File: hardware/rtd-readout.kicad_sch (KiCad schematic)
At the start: 32 parts, among them J1 Conn_RTD_4W, J4 Conn_T7_Analog, J5 Conn_T7_I2C, J6 Conn_Power, U1 ADS1115IDGS (0x48), U2 ADS1115IDGS (0x49)

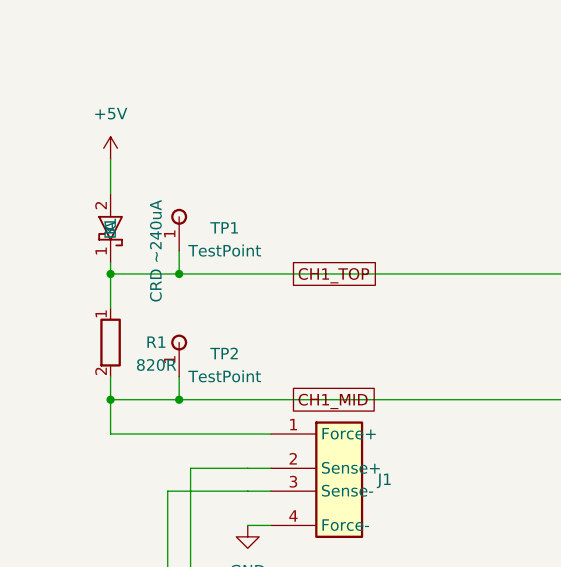
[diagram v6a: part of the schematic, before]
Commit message: rev-F: cryostat/stability respin - 100uA S-101T CRD, C0G sense path, 2ppm R_ref
Sensors are in a vacuum cryostat down to ~100 K; excitation lowered to cut
self-heating ~6x (0.3-1.6 uW nominal), measurement path upgraded to
precision-grade passives. All parts live-verified on Digi-Key with
adversarial fact-checks:
- D1-D4: LIS J500 TO-92 -> SEMITEC S-101T (100uA typ, band 0.05-0.21mA,
  SMD flat 2-lead); custom footprint from SEMITEC's recommended land
  pattern (1.2x1.6mm pads, 3.4mm centers, cathode-band marking).
- R_ref: 820R 10ppm -> 1.00k +/-0.05% +/-2ppm/C (Vishay TNPU12061K00AWEN00);
  V_ref 100mV nom, 210mV = 82% FS at band max. Reference is no longer the
  drift limiter (by design).
- C5-C8: X7R 0805 -> C0G/NP0 0.1uF 50V 1206 (Murata GRM31C5C1H104JA01L);
  moved east of J4 on B.Cu with routed stubs (1206 body cannot straddle
  the pin holes). R7-R14: 1% thick film -> 0.1% 25ppm thin film (Susumu).
- Sims: 100uA/1k/2ppm/VL 2.0/RTD window extended to 100 K (Pt100 29.5R);
  band sweeps 0.5-2.1x; t3 criterion re-gated to 'R_ref not limiting';
  t6 noise assumption made per-read (4-conversion average).

Gates: ERC 0/0, DRC 0 violations / 0 unconnected, SPICE 7/7 PASS.

Co-Authored-By: Claude Fable 5 <noreply@anthropic.com>
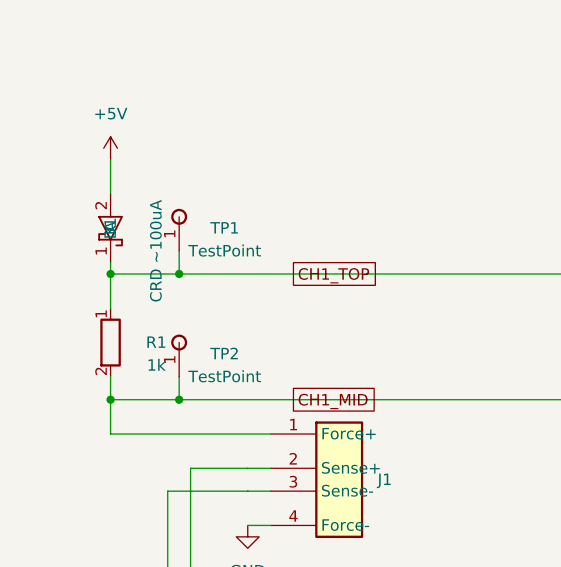
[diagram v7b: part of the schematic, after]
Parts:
- C5, C6, C7, C8: footprint rtd-readout:C_0805_2012Metric -> rtd-readout:C_1206_3216Metric; MPN CL21B104KBCNNNC -> GRM31C5C1H104JA01L; Manufacturer Samsung Electro-Mechanics -> Murata
- D1: value CRD ~240uA -> CRD ~100uA; footprint rtd-readout:TO-92-2_CRD-J500 -> rtd-readout:D_SEMITEC_S-101T; Current_nom ~0.24 mA (J500), +/-20% band (0.192-0.288 mA); stability ov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 -> ~0.10 mA typ (S-101T), band 0.05-0.21 mA (-50%/+110%); stab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; MPN J500 TO-92 2L -> S-101T; Manufacturer Linear Integrated Systems -> SEMITEC; Polarity Pin 1 = K (cathode). Pin 2 = A (anode). J500 TO-92 physical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 -> Pin 1 = K (cathode). Pin 2 = A (anode). S-101T physical: th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
- R1: value 820R -> 1k; MPN RN73H2BTTD8200B10 -> TNPU12061K00AWEN00
- R10, R11, R12, R13, R14, R7, R8, R9: MPN RC0805FR-071KL -> RG2012P-102-B-T5; Manufacturer Yageo -> Susumu
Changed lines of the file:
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@@
 			)
 		)
-		(property "Value" "CRD ~240uA"
+		(property "Value" "CRD ~100uA"
 			(at 43.18 48.26 0)
 			(show_name no)
@@
 			)
 		)
-		(property "Footprint" "rtd-readout:TO-92-2_CRD-J500"
+		(property "Footprint" "rtd-readout:D_SEMITEC_S-101T"
 			(at 38.1 45.72 0)
 			(show_name no)
@@
 			)
 		)
-		(property "Datasheet" "https://www.linearsystems.com/currentregulatingdiodes/j500-series"
+		(property "Datasheet" "https://www.semitec-global.com/uploads/2022/01/P22-23-CRD.pdf"
 			(at 38.1 45.72 0)
 			(show_name no)
@@
 			)
 		)
-		(property "Description" "Current-regulator diode (constant-current diode), ~0.24 mA (LIS J500, 0.192-0.288 mA band), two-terminal, TO-92 2-lead THT. Sets the per-channel excitation current; exact value is measured live and cancels (board_spec.md). Anode -> +V rail, cathode -> R_ref."
+		(property "Description" "Current-regulator diode (constant-current diode), ~0.10 mA (SEMITEC S-101T, 0.05-0.21 mA band), two-terminal, SMD flat 2-lead. rev-F: current lowered ~2.4x to cut RTD self-heating in the vacuum cryostat (sensors to ~100 K). Exact value is measured live and cancels (board_spec.md). Anode -> +V rail, cathode -> R_ref."
 			(at 38.1 45.72 0)
 			(show_name no)
@@
 			)
 		)
-		(property "MPN" "J500 TO-92 2L"
+		(property "MPN" "S-101T"
 			(at 38.1 45.72 0)
 			(show_name no)
@@
 			)
 		)
-		(property "Manufacturer" "Linear Integrated Systems"
+		(property "Manufacturer" "SEMITEC"
 			(at 38.1 45.72 0)
 			(show_name no)
@@
 			)
 		)
-		(property "Polarity" "Pin 1 = K (cathode). Pin 2 = A (anode). J500 TO-92 physical: facing the flat/marked face, left lead = A, right lead = K; the TO-92-2_CRD-J500 footprint silk is mirrored so matching the flat face to the silk outline puts K in pad 1."
+		(property "Polarity" "Pin 1 = K (cathode). Pin 2 = A (anode). S-101T physical: the CATHODE end carries a hatched band on the marked (top) face; place that band toward pad 1 (the silk bar + K marker side)."
 			(at 38.1 45.72 0)
 			(show_name no)
@@
 			)
 		)
-		(property "Current_nom" "~0.24 mA (J500), +/-20% band (0.192-0.288 mA); stability over one scan is what matters, not absolute value."
+		(property "Current_nom" "~0.10 mA typ (S-101T), band 0.05-0.21 mA (-50%/+110%); stability over one scan is what matters, not absolute value (huge spread and up to +2.1%/C Ip tempco are cancelled by the ratiometric readout)."
 			(at 38.1 45.72 0)
 			(show_name no)
@@
 			)
 		)
-		(property "ki_keywords" "CRD current regulator diode constant current J500 RTD excitation TO-92"
+		(property "ki_keywords" "CRD current regulator diode constant current SEMITEC S-101T RTD excitation SMD"
 			(at 38.1 45.72 0)
 			(show_name no)
@@
 			)
 		)
-		(property "ki_fp_filters" "TO?92*"
+		(property "ki_fp_filters" "D_SEMITEC*"
 			(at 38.1 45.72 0)
 			(show_name no)
@@
 			)
 		)
-		(property "Value" "820R"
+		(property "Value" "1k"
 			(at 43.18 60.96 0)
 			(show_name no)
@@
 			)
 		)
-		(property "Datasheet" "https://www.koaspeer.com/pdfs/RN73H.pdf"
+		(property "Datasheet" "https://www.vishay.com/docs/28779/tnpue3.pdf"
 			(at 38.1 58.42 0)
 			(show_name no)
@@
 			)
 		)
-		(property "Description" "Reference resistor for ratiometric current sense. 820 ohm sets V_ref ~197 mV nominal, <=236 mV at the J500 guaranteed-max 0.288 mA, inside the ADS1115 +/-0.256 V range. BINDING SPEC = tempco/stability, NOT absolute value (cross-cal constant C absorbs the value; board_spec.md s.R_ref)."
+		(property "Description" "Reference resistor for ratiometric current sense. 1.00 kohm sets V_ref ~100 mV nominal, <=210 mV at the S-101T band max 0.21 mA, inside the ADS1115 +/-0.256 V range. rev-F part is +/-2 ppm/C so R_ref is no longer the drift limiter. BINDING SPEC = tempco/stability, NOT absolute value (cross-cal absorbs the value; board_spec.md s.R_ref)."
 			(at 38.1 58.42 0)
 			(show_name no)
@@
 			)
 		)
-		(property "MPN" "RN73H2BTTD8200B10"
+		(property "MPN" "TNPU12061K00AWEN00"
 			(at 38.1 58.42 0)
 			(show_name no)
@@
 			)
 		)
-		(property "MPN" "RC0805FR-071KL"
+		(property "MPN" "RG2012P-102-B-T5"
 			(at 111.76 158.75 0)
 			(show_name no)
@@
 			)
 		)
-		(property "Manufacturer" "Yageo"
+		(property "Manufacturer" "Susumu"
 			(at 111.76 158.75 0)
 			(show_name no)
@@
 			)
 		)
-		(property "MPN" "RC0805FR-071KL"
+		(property "MPN" "RG2012P-102-B-T5"
 			(at 140.97 158.75 0)
 			(show_name no)
@@
 			)
 		)
-		(property "Manufacturer" "Yageo"
+		(property "Manufacturer" "Susumu"
 			(at 140.97 158.75 0)
 			(show_name no)
@@
 			)
 		)
-		(property "Footprint" "rtd-readout:C_0805_2012Metric"
+		(property "Footprint" "rtd-readout:C_1206_3216Metric"
 			(at 176.53 160.02 0)
 			(show_name no)
@@
 			)
 		)
-		(property "Description" "Generic non-polarized chip capacitor, 0805. Use for per-ADS1115 VDD decoupling (0.1 uF) and general bypass."
+		(property "Description" "Sense-line differential filter capacitor, 0.1 uF C0G/NP0 (Class 1: no DC-bias/temperature capacitance drift, no piezo, negligible dielectric absorption), 1206, 50 V. rev-F precision upgrade; sits directly in the measurement path with the 1 kohm filter resistors."
 			(at 176.53 160.02 0)
 			(show_name no)
@@
 			)
 		)
-		(property "MPN" "CL21B104KBCNNNC"
+		(property "MPN" "GRM31C5C1H104JA01L"
 			(at 176.53 160.02 0)
 			(show_name no)
@@
 			)
 		)
-		(property "Manufacturer" "Samsung Electro-Mechanics"
+		(property "Manufacturer" "Murata"
 			(at 176.53 160.02 0)
 			(show_name no)
@@
 			)
 		)
-		(property "MPN" "RC0805FR-071KL"
+		(property "MPN" "RG2012P-102-B-T5"
 			(at 111.76 162.56 0)
 			(show_name no)
@@
 			)
 		)
-		(property "Manufacturer" "Yageo"
+		(property "Manufacturer" "Susumu"
 			(at 111.76 162.56 0)
 			(show_name no)
@@
 			)
 		)
-		(property "MPN" "RC0805FR-071KL"
+		(property "MPN" "RG2012P-102-B-T5"
 			(at 140.97 162.56 0)
 			(show_name no)
@@
 			)
 		)
-		(property "Manufacturer" "Yageo"
+		(property "Manufacturer" "Susumu"
 			(at 140.97 162.56 0)
 			(show_name no)
@@
 			)
 		)
-		(property "Footprint" "rtd-readout:C_0805_2012Metric"
+		(property "Footprint" "rtd-readout:C_1206_3216Metric"
 			(at 176.53 163.83 0)
 			(show_name no)
@@
 			)
 		)
-		(property "Description" "Generic non-polarized chip capacitor, 0805. Use for per-ADS1115 VDD decoupling (0.1 uF) and general bypass."
+		(property "Description" "Sense-line differential filter capacitor, 0.1 uF C0G/NP0 (Class 1: no DC-bias/temperature capacitance drift, no piezo, negligible dielectric absorption), 1206, 50 V. rev-F precision upgrade; sits directly in the measurement path with the 1 kohm filter resistors."
 			(at 176.53 163.83 0)
 			(show_name no)
@@
 			)
 		)
-		(property "MPN" "CL21B104KBCNNNC"
+		(property "MPN" "GRM31C5C1H104JA01L"
 			(at 176.53 163.83 0)
 			(show_name no)
@@
 			)
 		)
-		(property "Manufacturer" "Samsung Electro-Mechanics"
+		(property "Manufacturer" "Murata"
 			(at 176.53 163.83 0)
 			(show_name no)
@@
 			)
 		)
-		(property "MPN" "RC0805FR-071KL"
+		(property "MPN" "RG2012P-102-B-T5"
 			(at 111.76 166.37 0)
 			(show_name no)
@@
 			)
 		)
-		(property "Manufacturer" "Yageo"
+		(property "Manufacturer" "Susumu"
 			(at 111.76 166.37 0)
 			(show_name no)
@@
 			)
 		)
-		(property "MPN" "RC0805FR-071KL"
+		(property "MPN" "RG2012P-102-B-T5"
 			(at 140.97 166.37 0)
 			(show_name no)
@@
 			)
 		)
-		(property "Manufacturer" "Yageo"
+		(property "Manufacturer" "Susumu"
 			(at 140.97 166.37 0)
 			(show_name no)
@@
 			)
 		)
-		(property "Footprint" "rtd-readout:C_0805_2012Metric"
+		(property "Footprint" "rtd-readout:C_1206_3216Metric"
 			(at 176.53 167.64 0)
 			(show_name no)
@@
 			)
 		)
-		(property "Description" "Generic non-polarized chip capacitor, 0805. Use for per-ADS1115 VDD decoupling (0.1 uF) and general bypass."
+		(property "Description" "Sense-line differential filter capacitor, 0.1 uF C0G/NP0 (Class 1: no DC-bias/temperature capacitance drift, no piezo, negligible dielectric absorption), 1206, 50 V. rev-F precision upgrade; sits directly in the measurement path with the 1 kohm filter resistors."
 			(at 176.53 167.64 0)
 			(show_name no)
@@
 			)
 		)
-		(property "MPN" "CL21B104KBCNNNC"
+		(property "MPN" "GRM31C5C1H104JA01L"
 			(at 176.53 167.64 0)
 			(show_name no)
@@
 			)
 		)
-		(property "Manufacturer" "Samsung Electro-Mechanics"
+		(property "Manufacturer" "Murata"
 			(at 176.53 167.64 0)
 			(show_name no)
@@
 			)
 		)
-		(property "MPN" "RC0805FR-071KL"
+		(property "MPN" "RG2012P-102-B-T5"
 			(at 111.76 173.99 0)
 			(show_name no)
@@
 			)
 		)
-		(property "Manufacturer" "Yageo"
+		(property "Manufacturer" "Susumu"
 			(at 111.76 173.99 0)
 			(show_name no)
@@
 			)
 		)
-		(property "MPN" "RC0805FR-071KL"
+		(property "MPN" "RG2012P-102-B-T5"
 			(at 140.97 173.99 0)
 			(show_name no)
@@
 			)
 		)
-		(property "Manufacturer" "Yageo"
+		(property "Manufacturer" "Susumu"
 			(at 140.97 173.99 0)
 			(show_name no)
@@
 			)
 		)
-		(property "Footprint" "rtd-readout:C_0805_2012Metric"
+		(property "Footprint" "rtd-readout:C_1206_3216Metric"
 			(at 176.53 175.26 0)
 			(show_name no)
@@
 			)
 		)
-		(property "Description" "Generic non-polarized chip capacitor, 0805. Use for per-ADS1115 VDD decoupling (0.1 uF) and general bypass."
+		(property "Description" "Sense-line differential filter capacitor, 0.1 uF C0G/NP0 (Class 1: no DC-bias/temperature capacitance drift, no piezo, negligible dielectric absorption), 1206, 50 V. rev-F precision upgrade; sits directly in the measurement path with the 1 kohm filter resistors."
 			(at 176.53 175.26 0)
 			(show_name no)
@@
 			)
 		)
-		(property "MPN" "CL21B104KBCNNNC"
+		(property "MPN" "GRM31C5C1H104JA01L"
 			(at 176.53 175.26 0)
 			(show_name no)
@@
 			)
 		)
-		(property "Manufacturer" "Samsung Electro-Mechanics"
+		(property "Manufacturer" "Murata"
 			(at 176.53 175.26 0)
 			(show_name no)

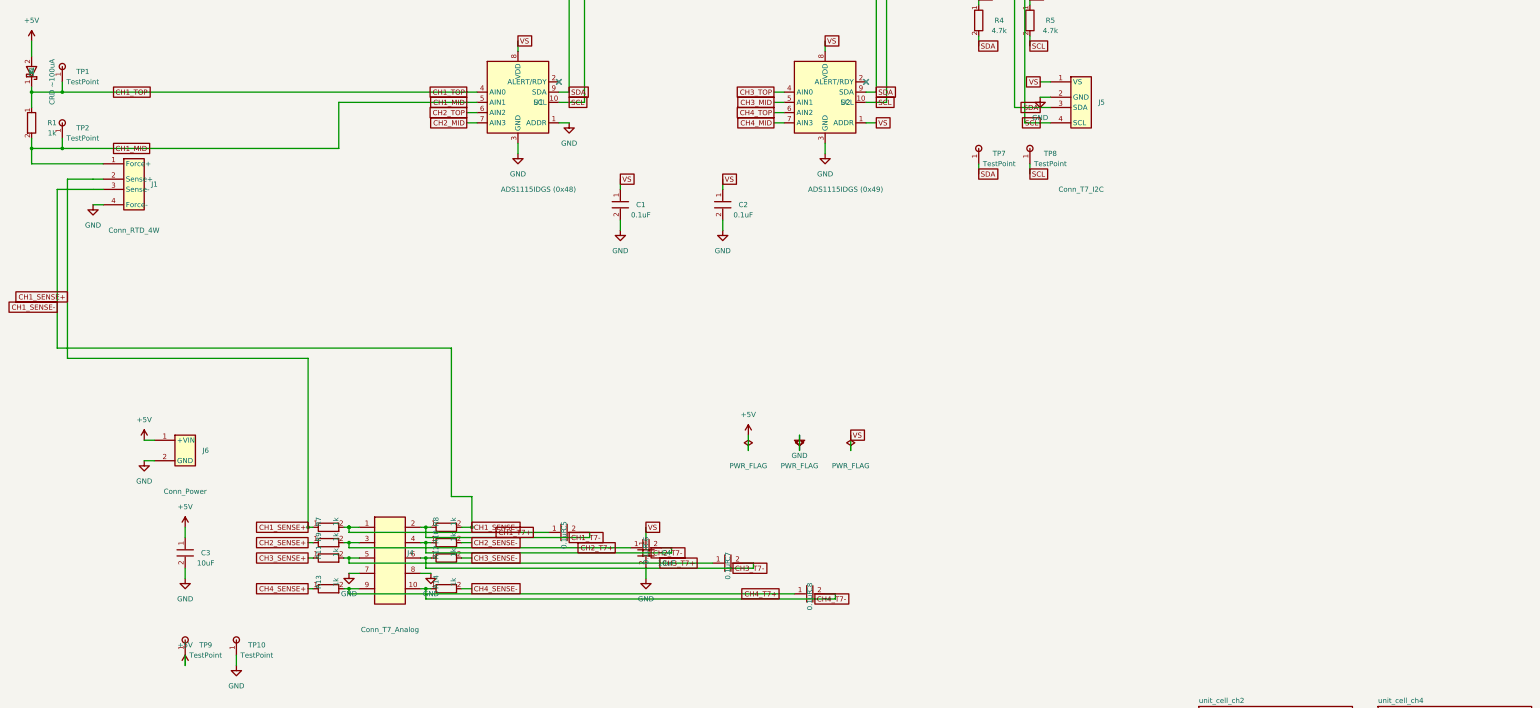
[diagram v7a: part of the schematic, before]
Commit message: rev-G: enclosure integration - 100x159.5 board, Hammond 1455N, RJ45/PT/KK I/O
Board resized to slide into a Hammond 1455N1601 extrusion (machinable end
panels, connectors proud/flush through cutouts). All parts live-verified
with adversarial fact-checks:
- RTD inputs: 4x Phoenix PT 1,5/5-3,5-H push-in blocks (pin 5 = cable
  shield to AGND); kept terminal blocks over RJ45 for bare cryo cables.
- T7 analog: Amphenol RJHSE-5380 shielded RA RJ45, T568 pair mapping
  (CH1=1/2, CH2=3/6, CH3=4/5, CH4=7/8), shield+chassis bond at the jack.
- T7 I2C: Molex KK 254 friction-lock header; pin numbers reversed (1<->4,
  2<->3) to make the fan planar - pigtail map in PANELS_AND_PINOUTS.md.
- Routing: via-free corridor (y 63-81) carries the 4 sense pairs to a C0G
  cap ladder + gated T568 fan; I2C as parallel diagonals; +5V south edge.
- Deliverables: docs/PANELS_AND_PINOUTS.md, panel machining DXFs, renders.

Gates: ERC 0/0, DRC 0 violations / 0 unconnected, SPICE 7/7 PASS.
DRC iteration trail: 92 -> 32 -> 8 -> 1 -> 0.

Co-Authored-By: Claude Fable 5 <noreply@anthropic.com>
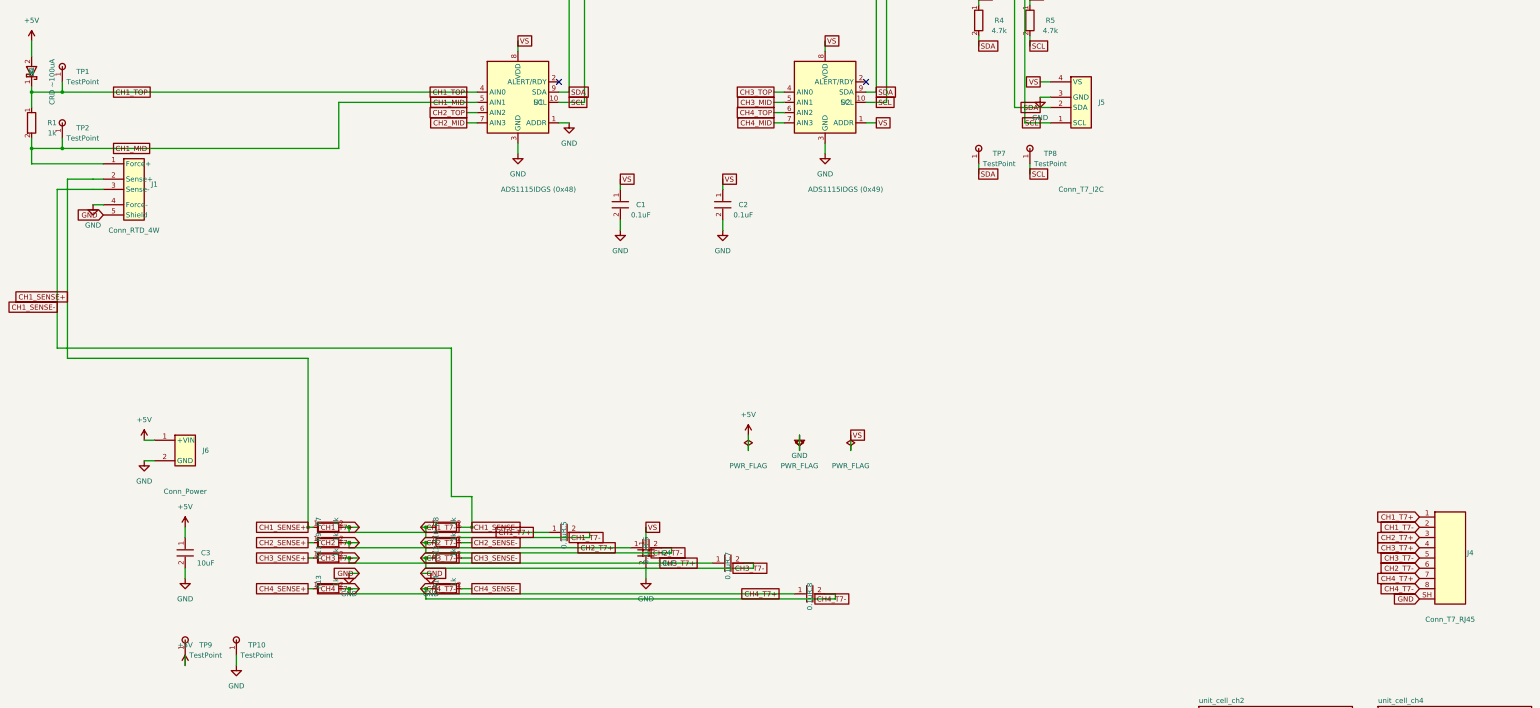
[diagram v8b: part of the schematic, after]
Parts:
- J1: footprint rtd-readout:TerminalBlock_Phoenix_MKDS-1,5-4-5.08_1x04_P5.08mm_Horizontal -> rtd-readout:TerminalBlock_Phoenix_PT-1,5-5-3.5-H_1x05_P3.50mm_Horizontal; MPN 1729144 (MKDS 1,5/4-5,08) -> 1984646 (PT 1,5/5-3,5-H); Manufacturer Phoenix Contact (or any 4-pos 5.08 mm screw terminal) -> Phoenix Contact (PT 1,5/5-3,5-H, 3.5 mm pitch; pin 5 = cabl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
- J4: value Conn_T7_Analog -> Conn_T7_RJ45; footprint rtd-readout:PinHeader_2x05_P2.54mm_Vertical -> rtd-readout:RJ45_Amphenol_RJHSE5380; symbol rtd-readout:Conn_T7_Analog -> rtd-readout:Conn_T7_RJ45; MPN PREC005DAAN-RC (2x5; confirm) -> RJHSE-5380; Manufacturer Sullins -> Amphenol CS (Commercial Products)
- J5: footprint rtd-readout:PinHeader_1x04_P2.54mm_Vertical -> rtd-readout:Molex_KK-254_AE-7395-04A_1x04_P2.54mm_Horizontal; MPN PREC004SAAN-RC -> 22-05-7048; Manufacturer Sullins -> Molex (KK 254; mate: housing 22-01-3047 + crimps 0008500160)
- J6: footprint rtd-readout:TerminalBlock_Phoenix_MKDS-1,5-2-5.08_1x02_P5.08mm_Horizontal -> rtd-readout:TerminalBlock_Phoenix_PT-1,5-2-3.5-H_1x02_P3.50mm_Horizontal; MPN 1729128 (MKDS 1,5/2-5,08) -> 1984617 (PT 1,5/2-3,5-H); Manufacturer Phoenix Contact (or any 2-pos 5.08 mm screw terminal) -> Phoenix Contact (PT 1,5/2-3,5-H, 3.5 mm pitch)
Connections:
- net CH2_T7-: now also J4.6 (CH2-); no longer J4.4 (CH2_Sense-)
- net CH3_T7+: now also J4.4 (CH3+); no longer J4.5 (CH3_Sense+)
- net CH3_T7-: now also J4.5 (CH3-); no longer J4.6 (CH3_Sense-)
- net CH4_T7+: now also J4.7 (CH4+); no longer J4.9 (CH4_Sense+)
- net CH4_T7-: now also J4.8 (CH4-); no longer J4.10 (CH4_Sense-)
- net GND: now also J1.5 (Shield), J4.SH (SHIELD), J5.3 (GND); no longer J4.7 (AGND), J4.8 (AGND), J5.2 (GND)
- net SCL: now also J5.1 (SCL); no longer J5.4 (SCL)
- net SDA: now also J5.2 (SDA); no longer J5.3 (SDA)
- net VS: now also J5.4 (VS); no longer J5.1 (VS)
